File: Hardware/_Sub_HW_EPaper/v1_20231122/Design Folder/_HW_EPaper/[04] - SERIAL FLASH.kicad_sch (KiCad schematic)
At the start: 5 parts, among them U401 W25Q64JVSSIQ

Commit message: EPaper schematic is almost done...
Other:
- moved on the sheet: R401, R402, R403

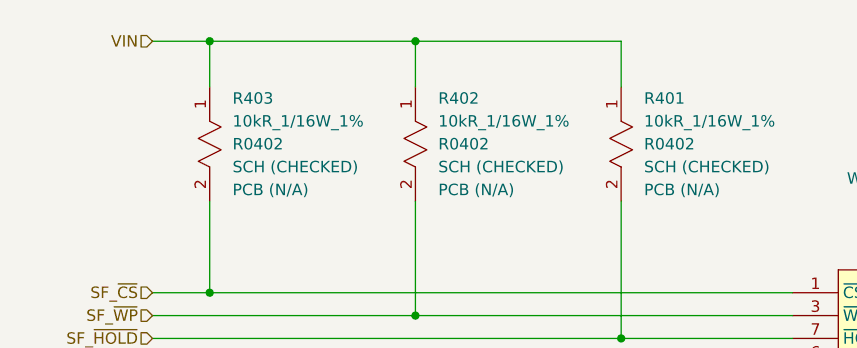
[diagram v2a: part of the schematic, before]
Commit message: Working on epaper hardware
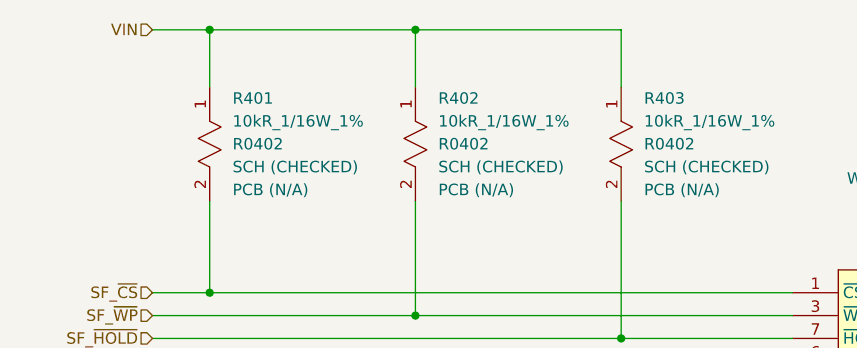
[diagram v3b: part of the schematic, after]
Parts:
- renumbered R403 to R401, R401 to R403
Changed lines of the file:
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@@
     (company "Mend0z0")
     (comment 1 "v1.0")
-    (comment 2 "PRELIMINARY")
+    (comment 2 "CHECKED")
   )
   (junction (at 147.32 120.65) (diameter 0) (color 0 0 0 0)
@@
   (junction (at 161.29 151.13) (diameter 0) (color 0 0 0 0)
   )
-  (junction (at 147.32 90.17) (diameter 0) (color 0 0 0 0)
+  (junction (at 147.32 88.9) (diameter 0) (color 0 0 0 0)
   )
   (junction (at 161.29 135.89) (diameter 0) (color 0 0 0 0)
@@
   (junction (at 170.18 123.19) (diameter 0) (color 0 0 0 0)
   )
-  (junction (at 124.46 90.17) (diameter 0) (color 0 0 0 0)
+  (junction (at 124.46 88.9) (diameter 0) (color 0 0 0 0)
   )
   (wire (pts (xy 118.11 118.11) (xy 124.46 118.11))
@@
     (stroke (width 0) (type default))
   )
-  (wire (pts (xy 124.46 90.17) (xy 124.46 95.25))
+  (wire (pts (xy 124.46 88.9) (xy 124.46 95.25))
     (stroke (width 0) (type default))
   )
@@
     (stroke (width 0) (type default))
   )
-  (wire (pts (xy 147.32 95.25) (xy 147.32 90.17))
+  (wire (pts (xy 147.32 95.25) (xy 147.32 88.9))
     (stroke (width 0) (type default))
   )
@@
     (stroke (width 0) (type default))
   )
-  (wire (pts (xy 170.18 95.25) (xy 170.18 90.17))
+  (wire (pts (xy 170.18 95.25) (xy 170.18 88.9))
     (stroke (width 0) (type default))
   )
@@
     (stroke (width 0) (type default))
   )
-  (wire (pts (xy 118.11 90.17) (xy 124.46 90.17))
-    (stroke (width 0) (type default))
-  )
-  (wire (pts (xy 147.32 90.17) (xy 124.46 90.17))
+  (wire (pts (xy 118.11 88.9) (xy 124.46 88.9))
+    (stroke (width 0) (type default))
+  )
+  (wire (pts (xy 147.32 88.9) (xy 124.46 88.9))
     (stroke (width 0) (type default))
   )
@@
     (stroke (width 0) (type default))
   )
-  (wire (pts (xy 170.18 90.17) (xy 147.32 90.17))
+  (wire (pts (xy 170.18 88.9) (xy 147.32 88.9))
     (stroke (width 0) (type default))
   )
@@
     (effects (font (size 1.27 1.27)) (justify right))
   )
-  (hierarchical_label "VIN" (shape input) (at 118.11 90.17 180) (fields_autoplaced)
+  (hierarchical_label "VIN" (shape input) (at 118.11 88.9 180) (fields_autoplaced)
     (effects (font (size 1.27 1.27)) (justify right))
   )
@@
   (symbol (lib_id "_SCHLIB_Epaper:RES_10kR_1/16W_1%_R0402") (at 124.46 95.25 270) (unit 1)
     (in_bom yes) (on_board yes) (dnp no) (fields_autoplaced)
-    (property "Reference" "R403" (at 127 96.52 90)
+    (property "Reference" "R401" (at 127 96.52 90)
       (effects (font (size 1.27 1.27)) (justify left))
     )
@@
       (project "_HW_EPaper"
         (path "/adfaa0ae-c952-44c7-bc24-1bfe8f9a84a3/4e346fc8-747a-4f3e-83e0-81c9211edb38/4b5c65ef-4d97-4734-b226-3d1b8f3d6a0d"
-          (reference "R403") (unit 1)
+          (reference "R401") (unit 1)
         )
       )
@@
   (symbol (lib_id "_SCHLIB_Epaper:RES_10kR_1/16W_1%_R0402") (at 170.18 95.25 270) (unit 1)
     (in_bom yes) (on_board yes) (dnp no) (fields_autoplaced)
-    (property "Reference" "R401" (at 172.72 96.52 90)
+    (property "Reference" "R403" (at 172.72 96.52 90)
       (effects (font (size 1.27 1.27)) (justify left))
     )
@@
       (project "_HW_EPaper"
         (path "/adfaa0ae-c952-44c7-bc24-1bfe8f9a84a3/4e346fc8-747a-4f3e-83e0-81c9211edb38/4b5c65ef-4d97-4734-b226-3d1b8f3d6a0d"
-          (reference "R401") (unit 1)
-        )
-      )
+          (reference "R403") (unit 1)
+        )
+      )

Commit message: Hardware is almost done
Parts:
- U401: footprint Package_SO:SOIC-8_5.23x5.23mm_P1.27mm -> Package_SO:SOIC-8_5.275x5.275mm_P1.27mm; SCH CHECK SCH (N/A) -> SCH (CHECKED)
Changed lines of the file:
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@@
       (effects (font (size 1.27 1.27)))
     )
-    (property "Footprint" "Package_SO:SOIC-8_5.23x5.23mm_P1.27mm" (at 191.77 99.06 0)
+    (property "Footprint" "Package_SO:SOIC-8_5.275x5.275mm_P1.27mm" (at 191.77 99.06 0)
       (effects (font (size 1.27 1.27)) (justify left) hide)
     )
@@
       (effects (font (size 1.27 1.27)))
     )
-    (property "SCH CHECK" "SCH (N/A)" (at 201.93 110.49 0)
+    (property "SCH CHECK" "SCH (CHECKED)" (at 201.93 110.49 0)
       (effects (font (size 1.27 1.27)))
     )

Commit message: Updating file templates and structures...
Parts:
- C401: Manufacturer (none) -> Murata Electronics; Part Number GRM155Z71A105KE01D -> (none); Part Number (Manufacturer) (none) -> GRM155Z71A105KE01D; Part Number (Vendor) (none) -> 490-GRM155Z71A105KE01DTR-ND; Vendor (none) -> Digikey
- R401, R402, R403: Manufacturer (none) -> Bourns Inc.; Part Number CR0402-FX-1002GLF -> (none); Part Number (Manufacturer) (none) -> CR0402-FX-1002GLF; Part Number (Vendor) (none) -> CR0402-FX-1002GLFTR-ND; Vendor (none) -> Digikey
- U401: Manufacturer (none) -> Winbond Electronics; Part Number W25Q64JVSSIQ -> (none); Part Number (Manufacturer) (none) -> W25Q64JVSSIQ; Part Number (Vendor) (none) -> W25Q64JVSSIQ-ND; Vendor (none) -> Digikey
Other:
- moved on the sheet: C401, R401, R402, R403, U401
